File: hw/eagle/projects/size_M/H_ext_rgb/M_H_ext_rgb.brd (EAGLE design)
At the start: 6 parts

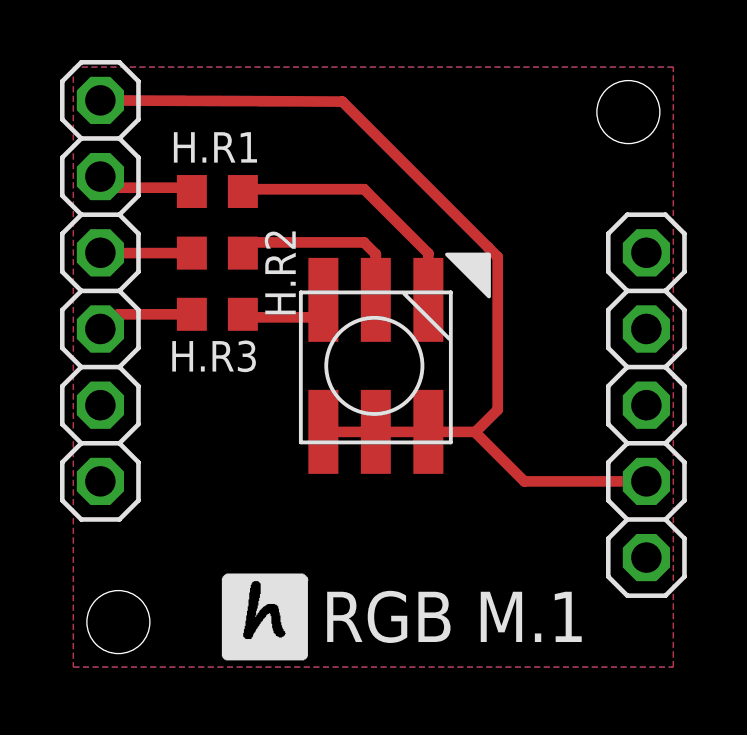
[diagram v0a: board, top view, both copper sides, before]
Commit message: updateed PCBs - adjustments based on usage of version 1
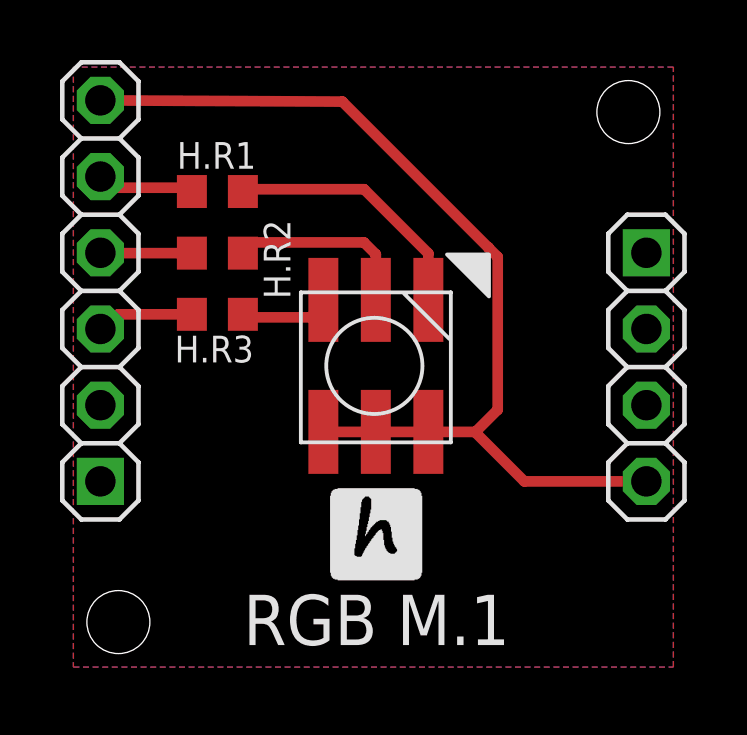
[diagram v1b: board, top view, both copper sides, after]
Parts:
- removed H.J3: (no value), pinhead2:1X05
- added JP1: (no value), pinhead2:1X04
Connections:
- net GND: now also JP1.4; no longer H.J3.4
- net VDD: now also JP1.3; no longer H.J3.3
